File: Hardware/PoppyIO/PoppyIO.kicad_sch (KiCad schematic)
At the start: 4 parts

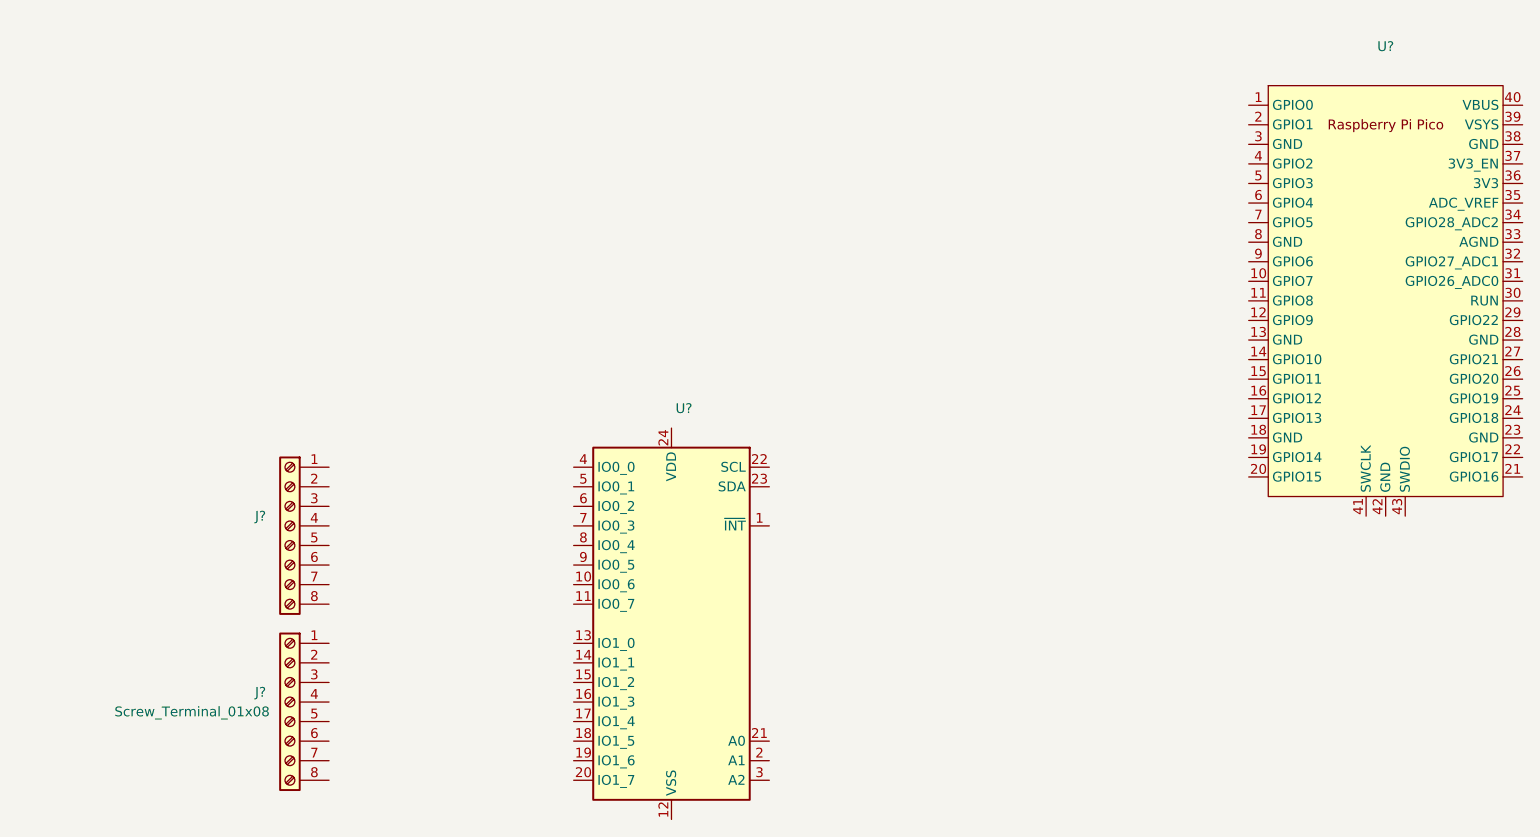
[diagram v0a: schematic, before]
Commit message: hw: io: Work on 24 VDC inputs and outputs
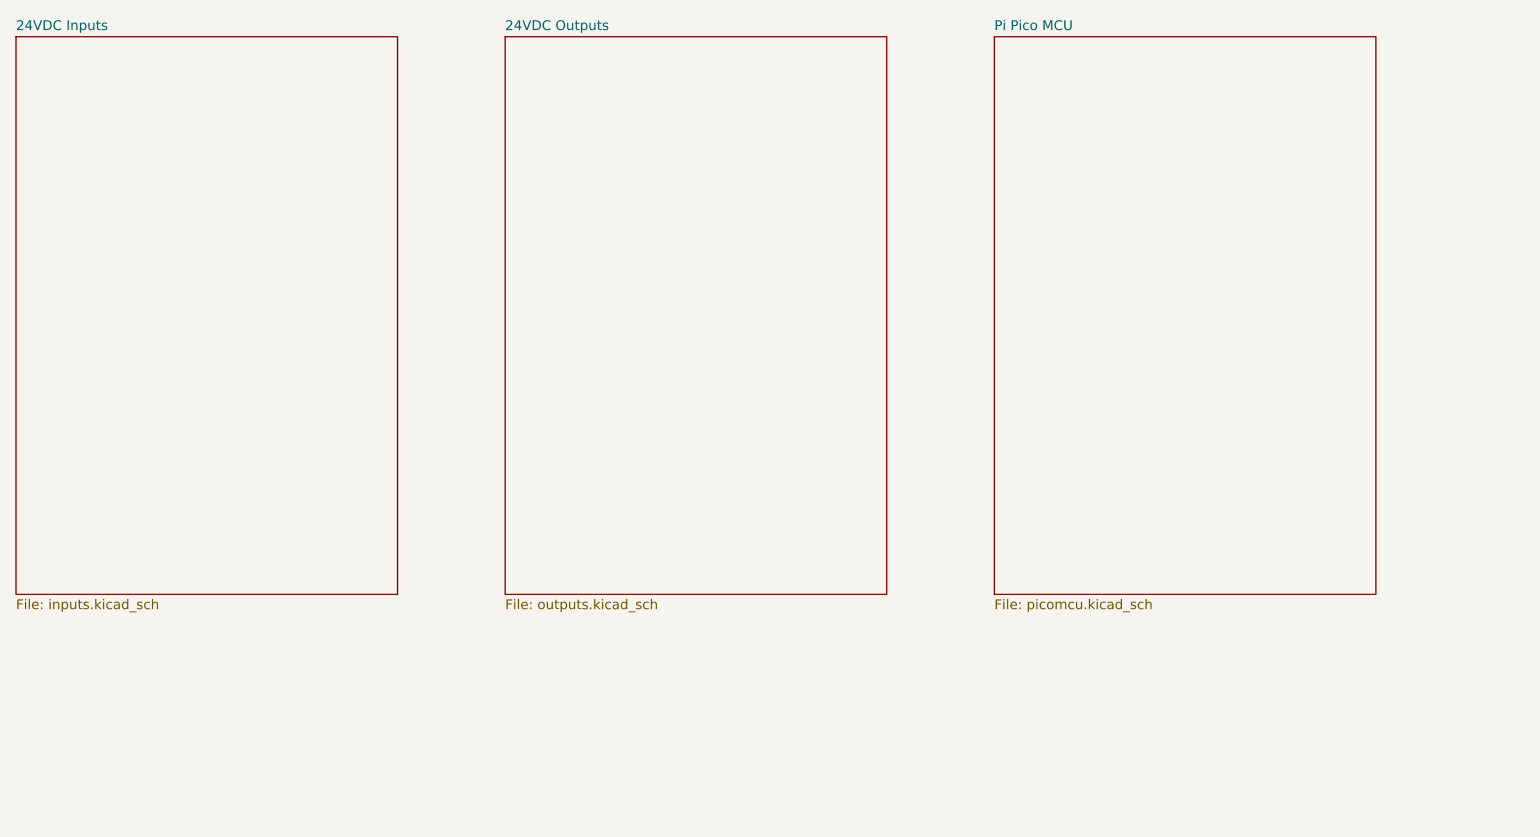
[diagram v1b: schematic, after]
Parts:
- removed J?: (no value), symbol Connector:Screw_Terminal_01x08
- removed J?: Screw_Terminal_01x08, symbol Connector:Screw_Terminal_01x08
- removed U?: (no value), symbol Interface_Expansion:PCA9555PW
- removed U?: (no value), symbol RPi_Pico:Pico
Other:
- added sheet 24VDC Inputs (inputs.kicad_sch)
- added sheet 24VDC Outputs (outputs.kicad_sch)
- added sheet Pi Pico MCU (picomcu.kicad_sch)

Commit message: hw: io: Updates
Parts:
- added J?: (no value), symbol Connector:Screw_Terminal_01x02
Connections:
- new net +5V: J?.1 (Pin_1)
- new net GND: J?.2 (Pin_2)

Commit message: hw: io: Single sheet
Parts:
- added C? (x2): (no value), symbol Device:C_Small
- added C? (x2): 100n, symbol Device:C_Small
- added D? (x16): Green, symbol Device:LED_Small
- added D?: (no value), symbol Device:D_Schottky_Small
- added J? (x8): WAGO 233-508, symbol Connector:Screw_Terminal_01x04
- added J?: WAGO 233-502, symbol Connector:Screw_Terminal_01x02
- added JP?: ~, symbol Jumper:Jumper_2_Bridged
- added Q? (x16): FC6946010R, symbol Device:Q_Dual_NMOS_S1G1D2S2G2D1
- added R? (x16): 680k, symbol Device:R_Small
- added R? (x16): 1k, symbol Device:R_Small
- added R? (x16): 100k, symbol Device:R_Small
- added R? (x2): DNP, symbol Device:R_Small
- added R?: (no value), symbol Device:R_Small
- added SW?: (no value), symbol Switch:SW_Push
- added TP? (x16): TestPoint, symbol Connector:TestPoint
- added U?: Pico, RPi_Pico:RPi_Pico_SMD_TH, symbol RPi_Pico:Pico
- added U? (x2): PCA9555PW, Package_SO:TSSOP-24_4.4x7.8mm_P0.65mm, symbol Interface_Expansion:PCA9555PW
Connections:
- net +5V: now also JP?.1 (A)
- net GND: now also C?.2, C?.2, C?.2, C?.2, J?.1 (Pin_1), J?.2 (Pin_2), Q?.1 (S), Q?.1 (S), Q?.1 (S), Q?.1 (S), Q?.1 (S), Q?.1 (S), Q?.1 (S), Q?.1 (S), Q?.4 (S), Q?.4 (S), Q?.4 (S), Q?.4 (S), Q?.4 (S), Q?.4 (S), Q?.4 (S), Q?.4 (S), R?.2, R?.2, R?.2, R?.2, R?.2, R?.2, R?.2, R?.2, R?.2, R?.2, R?.2, R?.2, R?.2, R?.2, R?.2, R?.2, SW?.2, U?.12 (VSS), U?.12 (VSS), U?.13 (GND), U?.18 (GND), U?.23 (GND), U?.28 (GND), U?.3 (GND), U?.33 (AGND), U?.38 (GND), U?.8 (GND)
- new net: D?.1 (K), R?.1 (x16)
- new net: Q?.3 (D), R?.2, TP?.1 (x8)
- new net: Q?.6 (D), R?.2, TP?.1 (x8)
- new net: C?.1, D?.2 (A), JP?.2 (B)
- new net +3V3: C?.1, C?.1, D?.2 (A), D?.2 (A), D?.2 (A), D?.2 (A), D?.2 (A), D?.2 (A), D?.2 (A), D?.2 (A), D?.2 (A), D?.2 (A), D?.2 (A), D?.2 (A), D?.2 (A), D?.2 (A), D?.2 (A), D?.2 (A), R?.1, R?.1, R?.1, U?.24 (VDD), U?.24 (VDD)
- new net I00_HIGH: J?.1 (Pin_1), R?.1
- new net I00_LOW: Q?.2 (G), R?.1, R?.2, U?.4 (IO0_0)
- new net I01_HIGH: J?.2 (Pin_2), R?.1
- new net I01_LOW: Q?.5 (G), R?.1, R?.2, U?.5 (IO0_1)
- new net I02_HIGH: J?.3 (Pin_3), R?.1
- new net I02_LOW: Q?.2 (G), R?.1, R?.2, U?.6 (IO0_2)
- new net I03_HIGH: J?.4 (Pin_4), R?.1
- new net I03_LOW: Q?.5 (G), R?.1, R?.2, U?.7 (IO0_3)
- new net I04_HIGH: J?.1 (Pin_1), R?.1
- new net I04_LOW: Q?.2 (G), R?.1, R?.2, U?.8 (IO0_4)
- new net I05_HIGH: J?.2 (Pin_2), R?.1
- new net I05_LOW: Q?.5 (G), R?.1, R?.2, U?.9 (IO0_5)
- new net I06_HIGH: J?.3 (Pin_3), R?.1
- new net I06_LOW: Q?.2 (G), R?.1, R?.2, U?.10 (IO0_6)
- new net I07_HIGH: J?.4 (Pin_4), R?.1
- new net I07_LOW: Q?.5 (G), R?.1, R?.2, U?.11 (IO0_7)
- new net I08_HIGH: J?.1 (Pin_1), R?.1
- new net I08_LOW: Q?.2 (G), R?.1, R?.2, U?.13 (IO1_0)
- new net I09_HIGH: J?.2 (Pin_2), R?.1
- new net I09_LOW: Q?.5 (G), R?.1, R?.2, U?.14 (IO1_1)
- new net I10_HIGH: J?.3 (Pin_3), R?.1
- new net I10_LOW: Q?.2 (G), R?.1, R?.2, U?.15 (IO1_2)
- new net I11_HIGH: J?.4 (Pin_4), R?.1
- new net I11_LOW: Q?.5 (G), R?.1, R?.2, U?.16 (IO1_3)
- new net I12_HIGH: J?.1 (Pin_1), R?.1
- new net I12_LOW: Q?.2 (G), R?.1, R?.2, U?.17 (IO1_4)
- new net I13_HIGH: J?.2 (Pin_2), R?.1
- new net I13_LOW: Q?.5 (G), R?.1, R?.2, U?.18 (IO1_5)
- new net I14_HIGH: J?.3 (Pin_3), R?.1
- new net I14_LOW: Q?.2 (G), R?.1, R?.2, U?.19 (IO1_6)
- new net I15_HIGH: J?.4 (Pin_4), R?.1
- new net I15_LOW: Q?.5 (G), R?.1, R?.2, U?.20 (IO1_7)
- new net IO_SCL: U?.22 (SCL), U?.22 (SCL)
- new net IO_SDA: U?.23 (SDA), U?.23 (SDA)
- new net O00_HIGH: J?.1 (Pin_1)
- new net O00_LOW: U?.4 (IO0_0)
- new net O01_HIGH: J?.2 (Pin_2)
- new net O01_LOW: U?.5 (IO0_1)
- new net O02_HIGH: J?.3 (Pin_3)
- new net O02_LOW: U?.6 (IO0_2)
- new net O03_HIGH: J?.4 (Pin_4)
- new net O03_LOW: U?.7 (IO0_3)
- new net O04_HIGH: J?.1 (Pin_1)
- new net O04_LOW: U?.8 (IO0_4)
- new net O05_HIGH: J?.2 (Pin_2)
- new net O05_LOW: U?.9 (IO0_5)
- new net O06_HIGH: J?.3 (Pin_3)
- new net O06_LOW: U?.10 (IO0_6)
- new net O07_HIGH: J?.4 (Pin_4)
- new net O07_LOW: U?.11 (IO0_7)
- new net O08_HIGH: J?.1 (Pin_1)
- new net O08_LOW: U?.13 (IO1_0)
- new net O09_HIGH: J?.2 (Pin_2)
- new net O09_LOW: U?.14 (IO1_1)
- new net O10_HIGH: J?.3 (Pin_3)
- new net O10_LOW: U?.15 (IO1_2)
- new net O11_HIGH: J?.4 (Pin_4)
- new net O11_LOW: U?.16 (IO1_3)
- new net O12_HIGH: J?.1 (Pin_1)
- new net O12_LOW: U?.17 (IO1_4)
- new net O13_HIGH: J?.2 (Pin_2)
- new net O13_LOW: U?.18 (IO1_5)
- new net O14_HIGH: J?.3 (Pin_3)
- new net O14_LOW: U?.19 (IO1_6)
- new net O15_HIGH: J?.4 (Pin_4)
- new net O15_LOW: U?.20 (IO1_7)
- new net VSYS: D?.1 (K), U?.39 (VSYS)
- new net ~{INT_INPUT}: R?.2, U?.1 (~{INT})
- new net ~{INT_OUTPUT}: R?.2, U?.1 (~{INT})
- new net ~{RESET}: C?.1, R?.2, SW?.1, U?.30 (RUN)
- no-connect marks 0 -> 6
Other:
- removed sheet 24VDC Inputs
- removed sheet 24VDC Outputs
- removed sheet Pi Pico MCU
- moved on the sheet: J?

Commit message: hw: io: Updates
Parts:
- added R? (x2): 4.7k, symbol Device:R_Small
- added TP? (x2): TestPoint, symbol Connector:TestPoint
- C?: value (none) -> 100n
- C?: value (none) -> 47u
- D?: value (none) -> MBR120
- J?: value (none) -> WAGO 233-502
- R?: value (none) -> 10k
- SW?: value (none) -> PTS645SH43SMTR92LFS; footprint (none) -> Button_Switch_SMD:SW_SPST_PTS645
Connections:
- net +3V3: now also U?.36 (3V3), R?.1, R?.1
- net IO_SCL: now also U?.27 (GPIO21), R?.2, TP?.1
- net IO_SDA: now also U?.26 (GPIO20), R?.2, TP?.1
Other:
- note added: "Board to Board Connector"
- note added: "Jumper should be removed if Pi Pico is not mounted."
- moved on the sheet: C?, D?, JP?

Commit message: hw: io: Output drivers and other things
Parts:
- removed J?: WAGO 233-502, symbol Connector:Screw_Terminal_01x02
- added C?: (no value), symbol Device:C_Small
- added C?: DNP, symbol Device:C_Small
- added D? (x16): Green, symbol Device:LED_Small
- added J?: WAGO 233-508, symbol Connector:Screw_Terminal_01x04
- added J?: (no value), symbol Connector_Generic:Conn_02x03_Odd_Even
- added R? (x16): 1k, symbol Device:R_Small
- added R? (x2): (no value), symbol Device:R_Small
- added R?: 0R, symbol Device:R_Small
- added U?: (no value), symbol Transistor_Array:ULQ2003A
- added U? (x2): ULQ2003A, symbol Transistor_Array:ULQ2003A
- JP?: value ~ -> (none)
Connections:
- net +3V3: now also J?.1 (Pin_1)
- net GND: now also U?.42 (GND), C?.2, C?.2, J?.3 (Pin_3), J?.4 (Pin_4), J?.5 (Pin_5), R?.2, R?.2, R?.2, R?.2, R?.2, R?.2, R?.2, R?.2, R?.2, R?.2, R?.2, R?.2, R?.2, R?.2, R?.2, R?.2, R?.2, U?.8 (GND), U?.8 (GND), U?.8 (GND)
- net O00_HIGH: now also U?.16 (O1)
- net O00_LOW: now also D?.2 (A), U?.1 (I1)
- net O01_HIGH: now also U?.15 (O2)
- net O01_LOW: now also D?.2 (A), U?.2 (I2)
- net O02_HIGH: now also U?.14 (O3)
- net O02_LOW: now also D?.2 (A), U?.3 (I3)
- net O03_HIGH: now also U?.13 (O4)
- net O03_LOW: now also D?.2 (A), U?.4 (I4)
- net O04_HIGH: now also U?.12 (O5)
- net O04_LOW: now also D?.2 (A), U?.5 (I5)
- net O05_HIGH: now also U?.11 (O6)
- net O05_LOW: now also D?.2 (A), U?.6 (I6)
- net O06_HIGH: now also U?.10 (O7)
- net O06_LOW: now also D?.2 (A), U?.7 (I7)
- net O07_HIGH: now also U?.16 (O1)
- net O07_LOW: now also D?.2 (A), U?.1 (I1)
- net O08_HIGH: now also U?.15 (O2)
- net O08_LOW: now also D?.2 (A), U?.2 (I2)
- net O09_HIGH: now also U?.14 (O3)
- net O09_LOW: now also D?.2 (A), U?.3 (I3)
- net O10_HIGH: now also U?.13 (O4)
- net O10_LOW: now also D?.2 (A), U?.4 (I4)
- net O11_HIGH: now also U?.12 (O5)
- net O11_LOW: now also D?.2 (A), U?.5 (I5)
- net O12_HIGH: now also U?.11 (O6)
- net O12_LOW: now also D?.2 (A), U?.6 (I6)
- net O13_HIGH: now also U?.10 (O7)
- net O13_LOW: now also D?.2 (A), U?.7 (I7)
- net O14_HIGH: now also U?.16 (O1)
- net O14_LOW: now also D?.2 (A), U?.1 (I1)
- net O15_HIGH: now also U?.15 (O2)
- net O15_LOW: now also D?.2 (A), U?.2 (I2)
- net ~{INT_INPUT}: now also R?.2
- net ~{INT_OUTPUT}: now also R?.2
- net ~{RESET}: now also J?.3 (Pin_3)
- net at U?.21 (GPIO16): now also C?.1, R?.1
- net at U?.22 (GPIO17): now also C?.1, R?.1
- net SWCLK: now reaches U?.41 (SWCLK)
- net SWCLK: now also J?.4 (Pin_4)
- net SWDIO: now reaches U?.43 (SWDIO)
- net SWDIO: now also J?.2 (Pin_2)
- new net: D?.1 (K), R?.1 (x16)
- new net: J?.6 (Pin_6), R?.1
- new net +24V: J?.1 (Pin_1), J?.2 (Pin_2), U?.9 (COM), U?.9 (COM), U?.9 (COM)
- no-connect marks 6 -> 3
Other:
- note added: "Configure as Inputs"
- note added: "Configure as Outputs"
- note added: "Tag-Connect Debug"
- moved on the sheet: C?, D?, J?, JP?, R?, SW?, TP?, U?

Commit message: hw: io: Annotate
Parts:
- added J12: (no value), symbol Connector_Generic:Conn_02x04_Counter_Clockwise
- added JP2: (no value), symbol Jumper:SolderJumper_2_Bridged
- added JP3, JP4, JP6, JP7: SolderJumper_2_Bridged, symbol Jumper:SolderJumper_2_Bridged
- added JP5: (no value), symbol Jumper:SolderJumper_2_Open
- U1: renamed from U?; value Pico -> (none)
- gave numbers to parts that had none: 155
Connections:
- net +3V3: now also J12.8 (Pin_8)
- net +5V: now also J12.1 (Pin_1)
- net GND: now also J12.4 (Pin_4), J12.5 (Pin_5), JP2.2 (B), JP3.2 (B), JP4.2 (B), JP5.2 (B), JP6.2 (B), JP7.2 (B)
- net IO_SCL: now also J12.7 (Pin_7)
- net IO_SDA: now also J12.6 (Pin_6)
- net ~{INT_INPUT}: now also J12.2 (Pin_2)
- net ~{INT_OUTPUT}: now also J12.3 (Pin_3)
- net at U2.2 (A1): now also JP3.1 (A)
- net at U2.21 (A0): now also JP2.1 (A)
- net at U2.3 (A2): now also JP4.1 (A)
- net at U3.2 (A1): now also JP6.1 (A)
- net at U3.21 (A0): now also JP5.1 (A)
- net at U3.3 (A2): now also JP7.1 (A)
- no-connect marks 3 -> 35
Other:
- moved on the sheet: J2

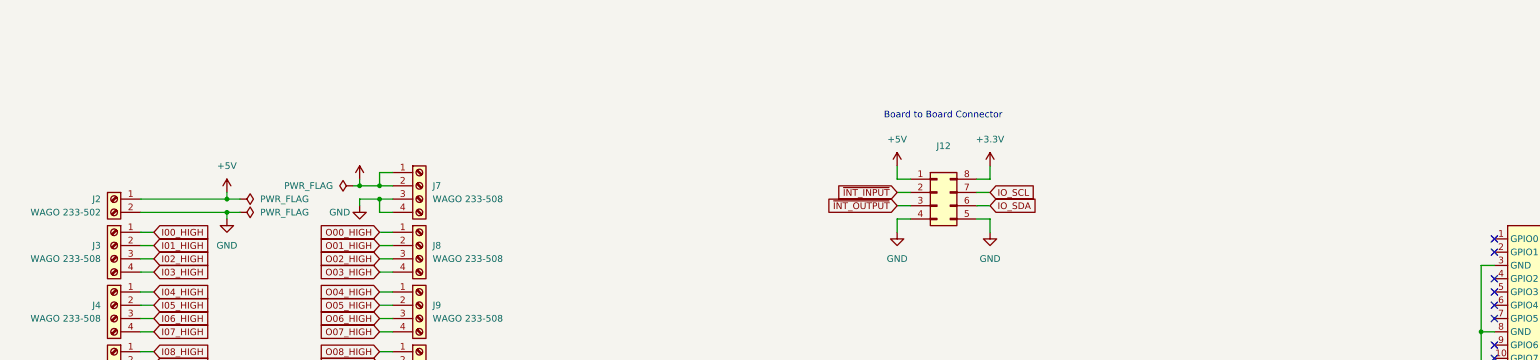
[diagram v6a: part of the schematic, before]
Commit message: hw: io: Footprints
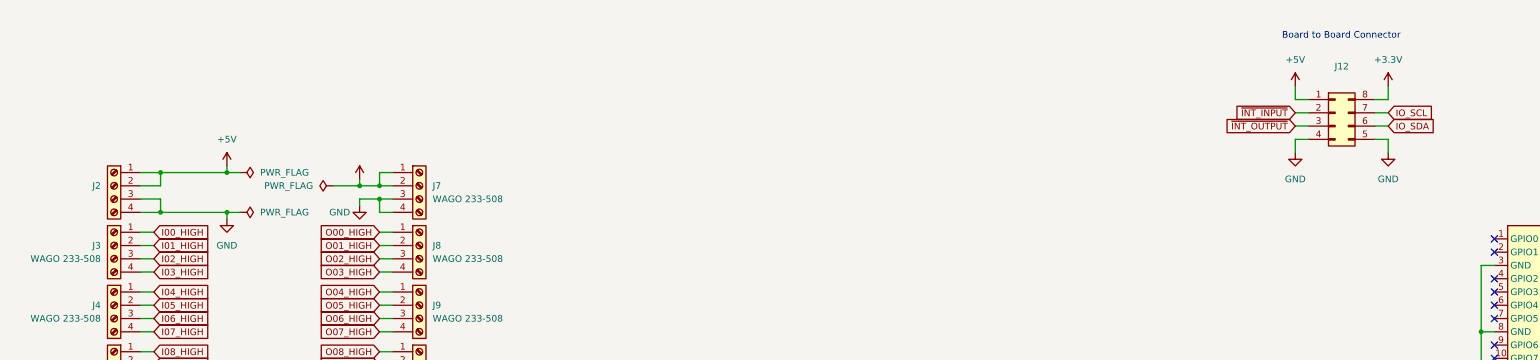
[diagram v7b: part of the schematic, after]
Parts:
- removed J2: WAGO 233-502, symbol Connector:Screw_Terminal_01x02
- added J2: (no value), symbol Connector:Screw_Terminal_01x04
- TP3: value TestPoint -> (none)
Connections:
- net +5V: now also J2.1 (Pin_1), J2.2 (Pin_2)
- net GND: now also J2.3 (Pin_3), J2.4 (Pin_4)
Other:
- moved on the sheet: J12

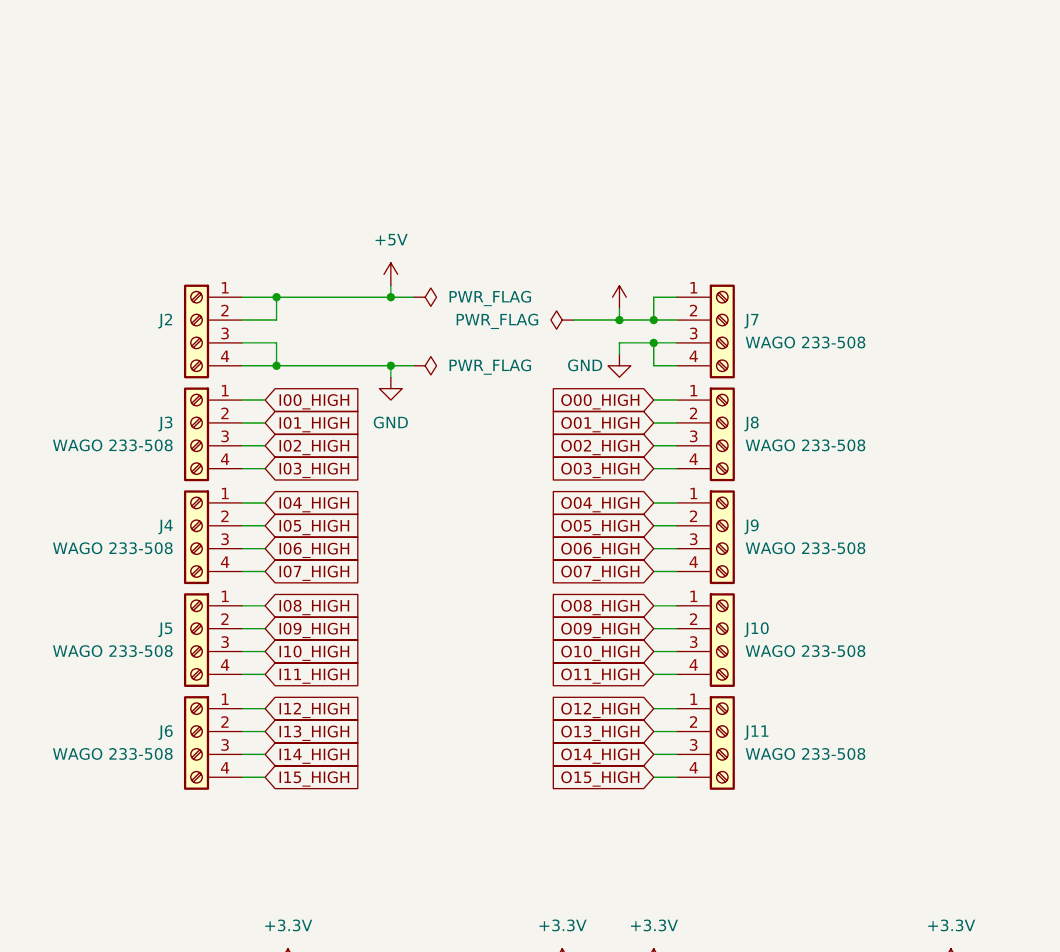
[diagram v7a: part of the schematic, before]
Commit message: hw: ui: Adjust connector pin ordering
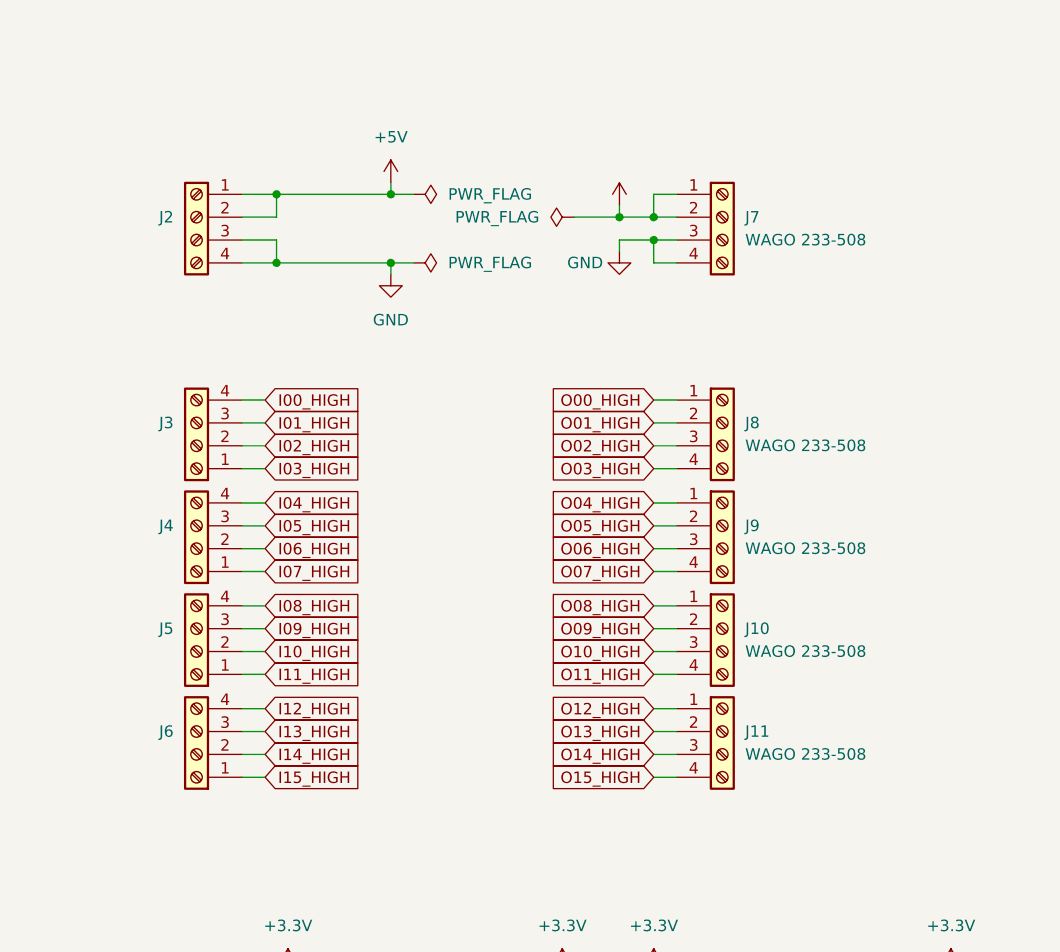
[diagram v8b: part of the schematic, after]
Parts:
- J3, J4, J5, J6: value WAGO 233-508 -> (none)
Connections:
- net I00_HIGH: now also J3.4 (Pin_4); no longer J3.1 (Pin_1)
- net I01_HIGH: now also J3.3 (Pin_3); no longer J3.2 (Pin_2)
- net I02_HIGH: now also J3.2 (Pin_2); no longer J3.3 (Pin_3)
- net I03_HIGH: now also J3.1 (Pin_1); no longer J3.4 (Pin_4)
- net I04_HIGH: now also J4.4 (Pin_4); no longer J4.1 (Pin_1)
- net I05_HIGH: now also J4.3 (Pin_3); no longer J4.2 (Pin_2)
- net I06_HIGH: now also J4.2 (Pin_2); no longer J4.3 (Pin_3)
- net I07_HIGH: now also J4.1 (Pin_1); no longer J4.4 (Pin_4)
- net I08_HIGH: now also J5.4 (Pin_4); no longer J5.1 (Pin_1)
- net I09_HIGH: now also J5.3 (Pin_3); no longer J5.2 (Pin_2)
- net I10_HIGH: now also J5.2 (Pin_2); no longer J5.3 (Pin_3)
- net I11_HIGH: now also J5.1 (Pin_1); no longer J5.4 (Pin_4)
- net I12_HIGH: now also J6.4 (Pin_4); no longer J6.1 (Pin_1)
- net I13_HIGH: now also J6.3 (Pin_3); no longer J6.2 (Pin_2)
- net I14_HIGH: now also J6.2 (Pin_2); no longer J6.3 (Pin_3)
- net I15_HIGH: now also J6.1 (Pin_1); no longer J6.4 (Pin_4)
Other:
- moved on the sheet: J2, J3, J4, J5, J6, J7
